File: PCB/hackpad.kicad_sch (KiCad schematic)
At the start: 6 parts, among them SW1 SW_Push, SW2 SW_Push, SW3 SW_Push, SW4 SW_Push, U1 MOUDLE-SEEEDUINO-XIAO

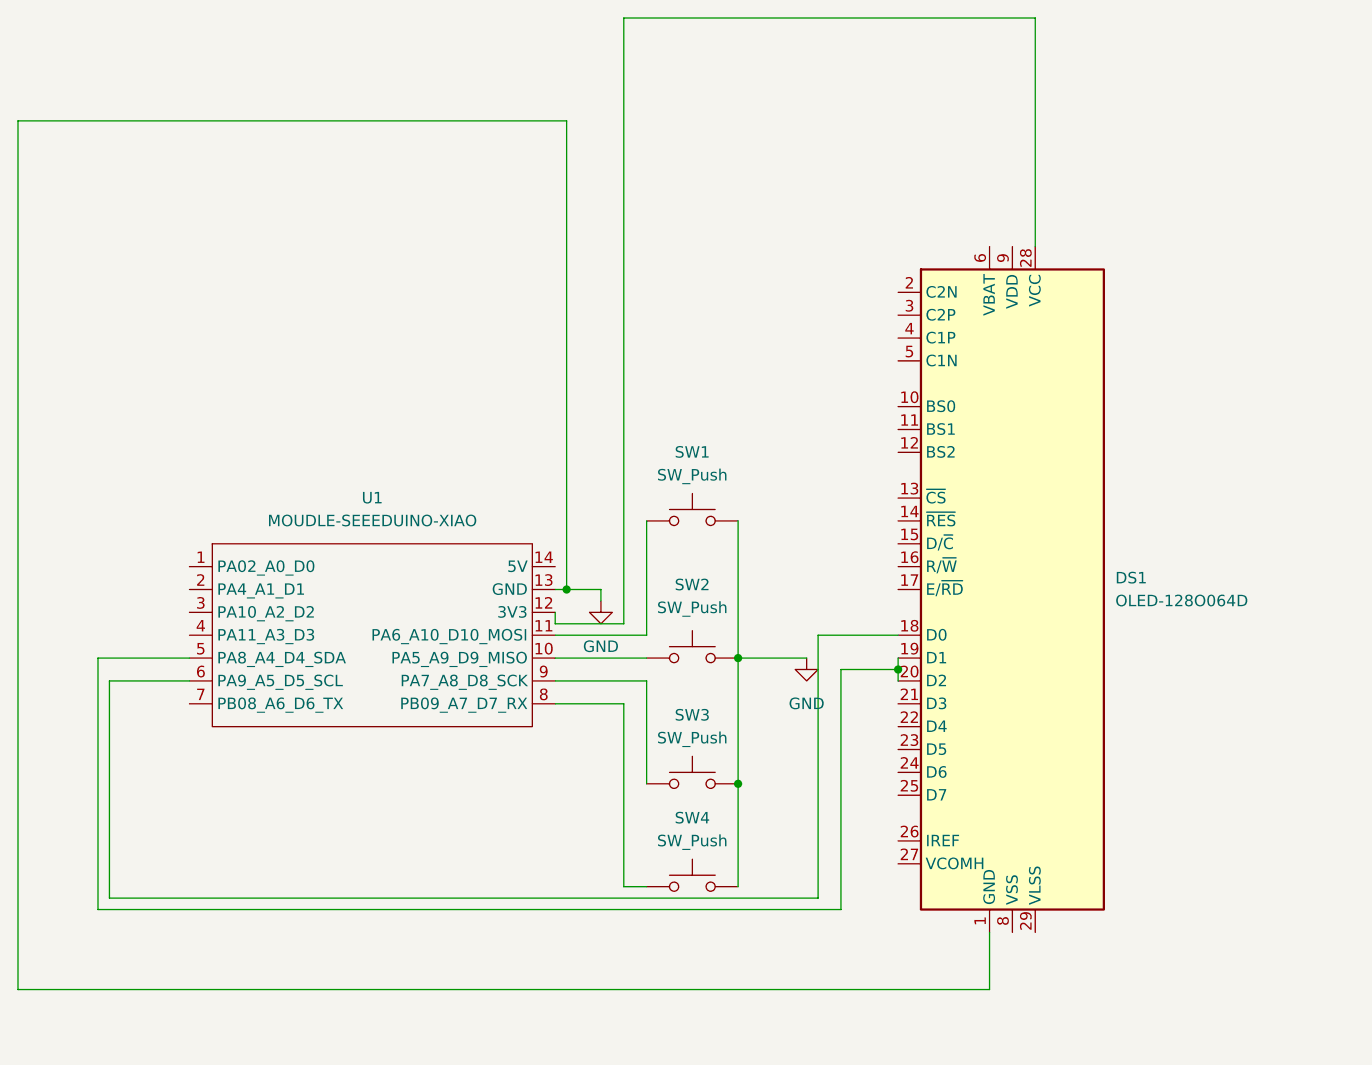
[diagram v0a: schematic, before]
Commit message: changed oled
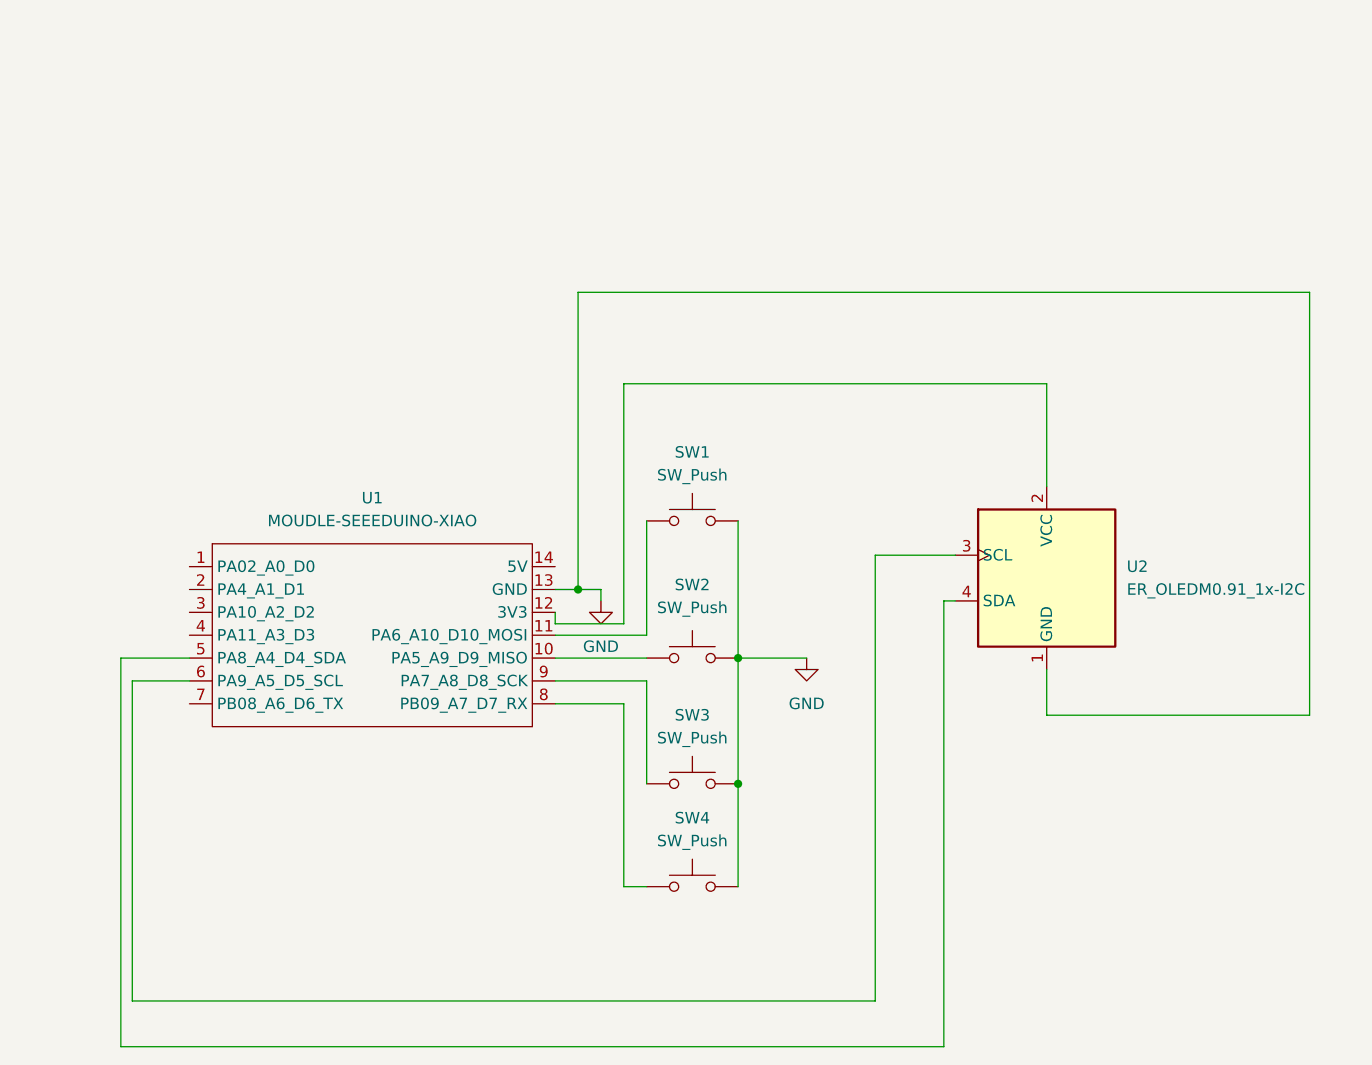
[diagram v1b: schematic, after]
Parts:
- removed DS1: OLED-128O064D, Display:OLED-128O064D, symbol Display_Graphic:OLED-128O064D
- added U2: ER_OLEDM0.91_1x-I2C, Display:ER_OLEDM0.91_1x-I2C, symbol Display_Graphic:ER_OLEDM0.91_1x-I2C
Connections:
- net GND: now also U2.1 (GND)
- net at U1.6 (PA9_A5_D5_SCL): now also U2.3 (SCL)
- net at U1.5 (PA8_A4_D4_SDA): now also U2.4 (SDA)
- net at U1.12 (3V3): now also U2.2 (VCC)
